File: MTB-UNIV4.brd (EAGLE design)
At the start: 100 x 80 mm, 27 parts, among them IC1 MEGA128-A, IC2 SN75176AP, IC3 NCP1117, IC4 ULN2803A, IC5 ULN2803A, X1 MKDSN1,5/4-5,08, X2 MKDSN1,5/4-5,08

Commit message: Přidány vstupní části
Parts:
- added C10, C11, C12, C13, C14, C15, C16, C17, C18, C19, C20, C21, C22, C23, C24, C9: 100nF, rcl:C1206
- added JP3, JP4: (no value), adafruit:1X08-BIG
- added R10, R11, R12, R13, R14, R15, R16, R17, R18, R3, R4, R5, R6, R7, R8, R9: 2k2, rcl:R1206
- added RN1, RN2: (no value), resistor-net:RN-9
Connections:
- new net N$21: C17.1, JP4.1, R11.2
- new net N$22: C18.1, JP4.2, R12.2
- new net N$23: C19.1, JP4.3, R13.2
- new net N$24: C20.1, JP4.4, R14.2
- new net N$25: C21.1, JP4.5, R15.2
- new net N$26: C22.1, JP4.6, R16.2
- new net N$27: C23.1, JP4.7, R17.2
- new net N$28: C24.1, JP4.8, R18.2
- new net N$29: C9.1, JP3.1, R3.2
- new net N$30: C10.1, JP3.2, R4.2
- new net N$31: C11.1, JP3.3, R5.2
- new net N$32: C12.1, JP3.4, R6.2
- new net N$33: C13.1, JP3.5, R7.2
- new net N$34: C14.1, JP3.6, R8.2
- new net N$35: C15.1, JP3.7, R9.2
- new net N$36: C16.1, JP3.8, R10.2
- net +5V: now also RN1.1, RN2.1
- net D-IN(A)1: now also R3.1, RN1.9
- net D-IN(A)2: now also R4.1, RN1.8
- net D-IN(A)3: now also R5.1, RN1.7
- net D-IN(A)4: now also R6.1, RN1.6
- net D-IN(A)5: now also R7.1, RN1.5
- net D-IN(A)6: now also R8.1, RN1.4
- net D-IN(A)7: now also R9.1, RN1.3
- net D-IN(A)8: now also R10.1, RN1.2
- net D-IN(B)1: now also R11.1, RN2.9
- net D-IN(B)2: now also R12.1, RN2.8
- net D-IN(B)3: now also R13.1, RN2.7
- net D-IN(B)4: now also R14.1, RN2.6
- net D-IN(B)5: now also R15.1, RN2.5
- net D-IN(B)6: now also R16.1, RN2.4
- net D-IN(B)7: now also R17.1, RN2.3
- net D-IN(B)8: now also R18.1, RN2.2
- net GND: now also C10.2, C11.2, C12.2, C13.2, C14.2, C15.2, C16.2, C17.2, C18.2, C19.2, C20.2, C21.2, C22.2, C23.2, C24.2, C9.2

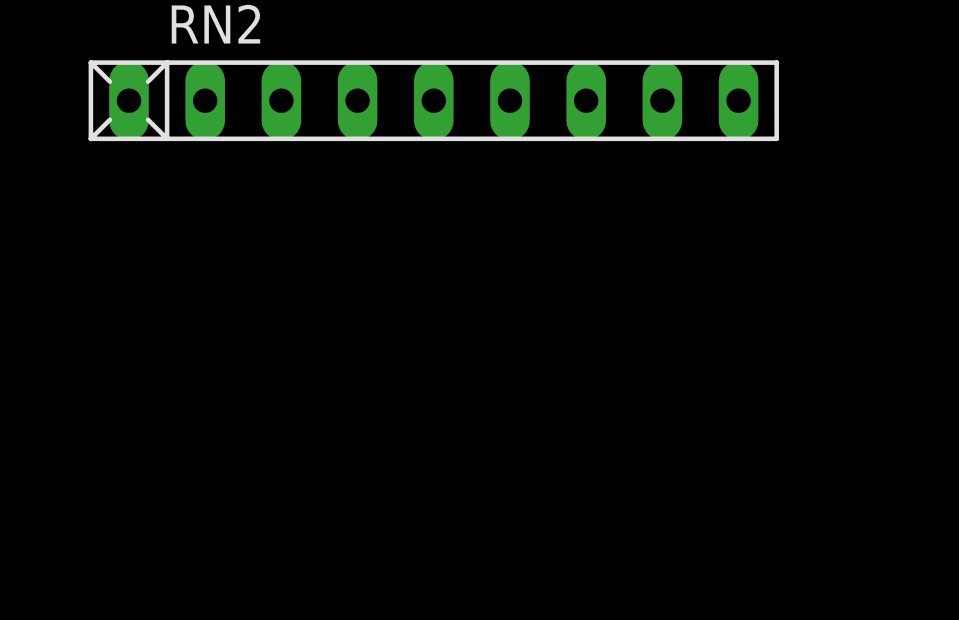
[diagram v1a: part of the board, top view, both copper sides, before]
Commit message: Přidány jumpery pro adresaci na sběrnici
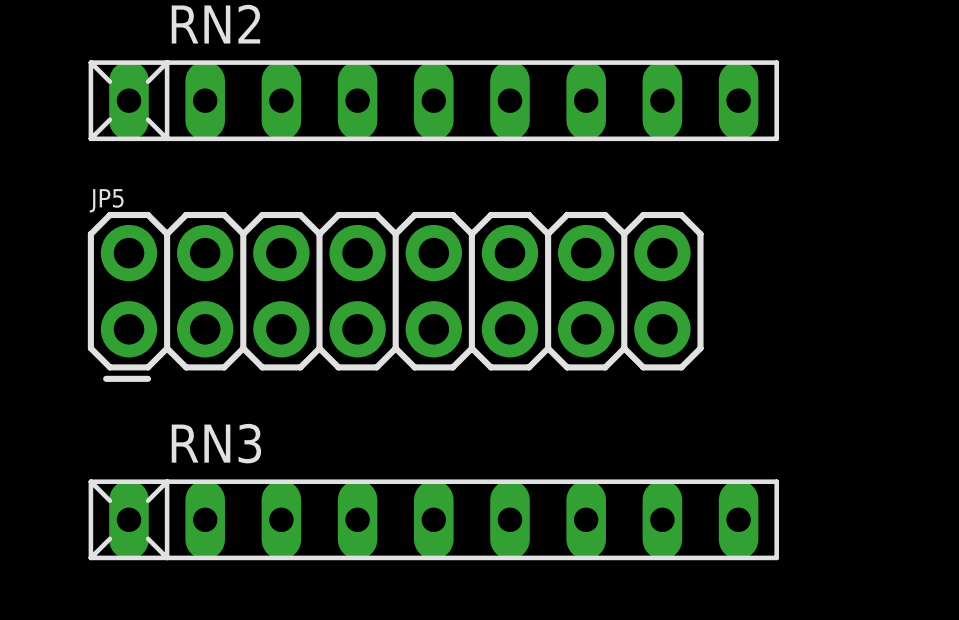
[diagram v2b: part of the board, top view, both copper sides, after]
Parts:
- added JP5: (no value), SparkFun-Connectors:2X8
- added RN3: 10k, resistor-net:RN-9
- RN1, RN2: value (none) -> 10k
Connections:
- new net ADDR-1: IC1.5, JP5.1, RN3.9
- new net ADDR-2: IC1.6, JP5.3, RN3.8
- new net ADDR-3: IC1.7, JP5.5, RN3.7
- new net ADDR-4: IC1.8, JP5.7, RN3.6
- new net ADDR-5: IC1.9, JP5.9, RN3.5
- new net ADDR-6: IC1.10, JP5.11, RN3.4
- new net ADDR-7: IC1.14, JP5.13, RN3.3
- new net ADDR-8: IC1.15, JP5.15, RN3.2
- net +5V: now also RN3.1
- net GND: now also JP5.10, JP5.12, JP5.14, JP5.16, JP5.2, JP5.4, JP5.6, JP5.8
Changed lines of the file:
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@@
 <layer number="112" name="tSilk" color="7" fill="1" visible="no" active="yes"/>
 <layer number="113" name="ReferenceLS" color="7" fill="1" visible="no" active="no"/>
+<layer number="114" name="Badge_Outline" color="7" fill="1" visible="yes" active="yes"/>
+<layer number="115" name="ReferenceISLANDS" color="7" fill="1" visible="yes" active="yes"/>
 <layer number="116" name="Patch_BOT" color="9" fill="4" visible="no" active="yes"/>
 <layer number="118" name="Rect_Pads" color="7" fill="1" visible="no" active="no"/>
@@
 <attribute name="VALUE" x="-74.93" y="-422.91" size="1.27" layer="27"/>
 </element>
-<element name="RN1" library="resistor-net" library_urn="urn:adsk.eagle:library:343" package="RN-9" package3d_urn="urn:adsk.eagle:package:24977/1" value="" x="-64.77" y="-427.99" smashed="yes">
+<element name="RN1" library="resistor-net" library_urn="urn:adsk.eagle:library:343" package="RN-9" package3d_urn="urn:adsk.eagle:package:24977/1" value="10k" x="-64.77" y="-427.99" smashed="yes">
 <attribute name="MF" value="" x="-64.77" y="-427.99" size="1.778" layer="27" display="off"/>
 <attribute name="MPN" value="" x="-64.77" y="-427.99" size="1.778" layer="27" display="off"/>
@@
 <attribute name="VALUE" x="-73.66" y="-431.165" size="1.27" layer="27" ratio="10"/>
 </element>
-<element name="RN2" library="resistor-net" library_urn="urn:adsk.eagle:library:343" package="RN-9" package3d_urn="urn:adsk.eagle:package:24977/1" value="" x="-64.77" y="-434.34" smashed="yes">
+<element name="RN2" library="resistor-net" library_urn="urn:adsk.eagle:library:343" package="RN-9" package3d_urn="urn:adsk.eagle:package:24977/1" value="10k" x="-64.77" y="-434.34" smashed="yes">
 <attribute name="MF" value="" x="-64.77" y="-434.34" size="1.778" layer="27" display="off"/>
 <attribute name="MPN" value="" x="-64.77" y="-434.34" size="1.778" layer="27" display="off"/>
@@
 <attribute name="POPULARITY" value="1" x="-64.77" y="-434.34" size="1.778" layer="27" display="off"/>
 <attribute name="VALUE" x="-73.66" y="-437.515" size="1.27" layer="27" ratio="10"/>
+</element>
+<element name="JP5" library="SparkFun-Connectors" library_urn="urn:adsk.eagle:library:513" package="2X8" package3d_urn="urn:adsk.eagle:package:38152/1" value="" x="-74.93" y="-441.96" smashed="yes">
+<attribute name="NAME" x="-76.2" y="-437.896" size="0.6096" layer="25" font="vector" ratio="20"/>
+<attribute name="VALUE" x="-76.2" y="-444.373" size="0.6096" layer="27" font="vector" ratio="20"/>
+</element>
+<element name="RN3" library="resistor-net" library_urn="urn:adsk.eagle:library:343" package="RN-9" package3d_urn="urn:adsk.eagle:package:24977/1" value="10k" x="-64.77" y="-448.31" smashed="yes">
+<attribute name="MF" value="" x="-64.77" y="-448.31" size="1.778" layer="27" display="off"/>
+<attribute name="MPN" value="" x="-64.77" y="-448.31" size="1.778" layer="27" display="off"/>
+<attribute name="NAME" x="-73.66" y="-446.405" size="1.27" layer="25" ratio="10"/>
+<attribute name="OC_FARNELL" value="unknown" x="-64.77" y="-448.31" size="1.778" layer="27" display="off"/>
+<attribute name="OC_NEWARK" value="unknown" x="-64.77" y="-448.31" size="1.778" layer="27" display="off"/>
+<attribute name="POPULARITY" value="1" x="-64.77" y="-448.31" size="1.778" layer="27" display="off"/>
+<attribute name="VALUE" x="-73.66" y="-451.485" size="1.27" layer="27" ratio="10"/>
 </element>
 </elements>
@@
 <contactref element="C23" pad="2"/>
 <contactref element="C24" pad="2"/>
+<contactref element="JP5" pad="16"/>
+<contactref element="JP5" pad="14"/>
+<contactref element="JP5" pad="12"/>
+<contactref element="JP5" pad="10"/>
+<contactref element="JP5" pad="8"/>
+<contactref element="JP5" pad="6"/>
+<contactref element="JP5" pad="4"/>
+<contactref element="JP5" pad="2"/>
+<wire x1="-64.77" y1="-439.42" x2="-67.31" y2="-439.42" width="0" layer="19" extent="1-1"/>
+<wire x1="-62.23" y1="-439.42" x2="-64.77" y2="-439.42" width="0" layer="19" extent="1-1"/>
+<wire x1="-59.69" y1="-439.42" x2="-62.23" y2="-439.42" width="0" layer="19" extent="1-1"/>
+<wire x1="-57.15" y1="-439.42" x2="-59.69" y2="-439.42" width="0" layer="19" extent="1-1"/>
+<wire x1="-69.85" y1="-439.42" x2="-67.31" y2="-439.42" width="0" layer="19" extent="1-1"/>
+<wire x1="-72.39" y1="-439.42" x2="-69.85" y2="-439.42" width="0" layer="19" extent="1-1"/>
+<wire x1="-74.93" y1="-439.42" x2="-72.39" y2="-439.42" width="0" layer="19" extent="1-1"/>
+<wire x1="-72.26" y1="-420.37" x2="-72.39" y2="-439.42" width="0" layer="19" extent="1-1"/>
 <wire x1="-72.26" y1="-414.02" x2="-72.26" y2="-420.37" width="0" layer="19" extent="1-1"/>
 <wire x1="-72.26" y1="-407.67" x2="-72.26" y2="-414.02" width="0" layer="19" extent="1-1"/>
@@
 <contactref element="RN2" pad="1"/>
 <contactref element="RN1" pad="1"/>
+<contactref element="RN3" pad="1"/>
 <wire x1="-74.93" y1="-434.34" x2="-74.93" y2="-427.99" width="0" layer="19" extent="1-1"/>
+<wire x1="-74.93" y1="-448.31" x2="-74.93" y2="-434.34" width="0" layer="19" extent="1-1"/>
 <wire x1="-75.06" y1="-199.39" x2="-74.93" y2="-427.99" width="0" layer="19" extent="1-1"/>
 <wire x1="-76.43" y1="-184.15" x2="-75.06" y2="-199.39" width="0" layer="19" extent="1-1"/>
@@
 <wire x1="-57.15" y1="-207.01" x2="-72.238" y2="-267.97" width="0" layer="19" extent="1-1"/>
 </signal>
+<signal name="ADDR-1">
+<contactref element="IC1" pad="5"/>
+<contactref element="JP5" pad="1"/>
+<contactref element="RN3" pad="9"/>
+<wire x1="-74.93" y1="-441.96" x2="-54.61" y2="-448.31" width="0" layer="19" extent="1-1"/>
+<wire x1="-26.85" y1="-18.79" x2="-74.93" y2="-441.96" width="0" layer="19" extent="1-1"/>
+</signal>
+<signal name="ADDR-2">
+<contactref element="IC1" pad="6"/>
+<contactref element="JP5" pad="3"/>
+<contactref element="RN3" pad="8"/>
+<wire x1="-72.39" y1="-441.96" x2="-57.15" y2="-448.31" width="0" layer="19" extent="1-1"/>
+<wire x1="-26.85" y1="-19.59" x2="-72.39" y2="-441.96" width="0" layer="19" extent="1-1"/>
+</signal>
+<signal name="ADDR-3">
+<contactref element="IC1" pad="7"/>
+<contactref element="JP5" pad="5"/>
+<contactref element="RN3" pad="7"/>
+<wire x1="-69.85" y1="-441.96" x2="-59.69" y2="-448.31" width="0" layer="19" extent="1-1"/>
+<wire x1="-26.85" y1="-20.39" x2="-69.85" y2="-441.96" width="0" layer="19" extent="1-1"/>
+</signal>
+<signal name="ADDR-4">
+<contactref element="IC1" pad="8"/>
+<contactref element="JP5" pad="7"/>
+<contactref element="RN3" pad="6"/>
+<wire x1="-67.31" y1="-441.96" x2="-26.85" y2="-21.19" width="0" layer="19" extent="1-1"/>
+<wire x1="-62.23" y1="-448.31" x2="-67.31" y2="-441.96" width="0" layer="19" extent="1-1"/>
+</signal>
+<signal name="ADDR-5">
+<contactref element="IC1" pad="9"/>
+<contactref element="JP5" pad="9"/>
+<contactref element="RN3" pad="5"/>
+<wire x1="-64.77" y1="-448.31" x2="-64.77" y2="-441.96" width="0" layer="19" extent="1-1"/>
+<wire x1="-26.85" y1="-21.99" x2="-64.77" y2="-441.96" width="0" layer="19" extent="1-1"/>
+</signal>
+<signal name="ADDR-6">
+<contactref element="IC1" pad="10"/>
+<contactref element="JP5" pad="11"/>
+<contactref element="RN3" pad="4"/>
+<wire x1="-67.31" y1="-448.31" x2="-62.23" y2="-441.96" width="0" layer="19" extent="1-1"/>
+<wire x1="-26.85" y1="-22.79" x2="-62.23" y2="-441.96" width="0" layer="19" extent="1-1"/>
+</signal>
+<signal name="ADDR-7">
+<contactref element="IC1" pad="14"/>
+<contactref element="JP5" pad="13"/>
+<contactref element="RN3" pad="3"/>
+<wire x1="-69.85" y1="-448.31" x2="-59.69" y2="-441.96" width="0" layer="19" extent="1-1"/>
+<wire x1="-26.85" y1="-25.99" x2="-59.69" y2="-441.96" width="0" layer="19" extent="1-1"/>
+</signal>
+<signal name="ADDR-8">
+<contactref element="IC1" pad="15"/>
+<contactref element="JP5" pad="15"/>
+<contactref element="RN3" pad="2"/>
+<wire x1="-72.39" y1="-448.31" x2="-57.15" y2="-441.96" width="0" layer="19" extent="1-1"/>
+<wire x1="-26.85" y1="-26.79" x2="-57.15" y2="-441.96" width="0" layer="19" extent="1-1"/>
+</signal>
 </signals>

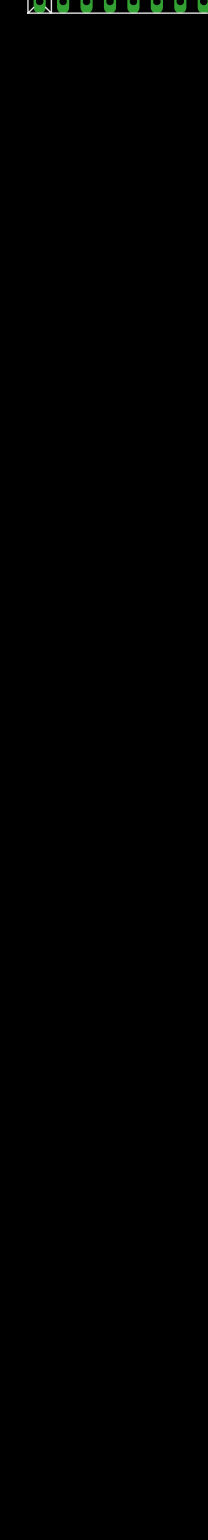
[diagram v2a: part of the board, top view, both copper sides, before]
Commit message: Nahradil jsem spojení COM na ULN Crowbar přepěťovou ochranou. Je to trochu více součástek, ale rozhodně to bude fungovat.
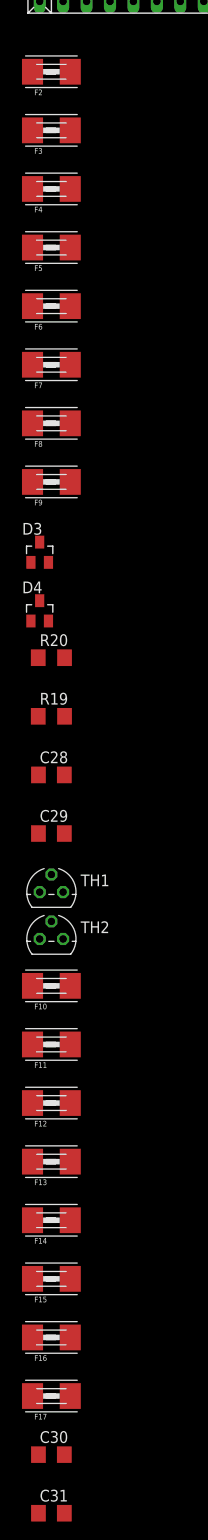
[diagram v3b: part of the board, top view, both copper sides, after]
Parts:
- added C28, C29, C30, C31: 100nF, rcl:C1206
- added D3, D4: (no value), diode:SOT23
- added F10, F11, F12, F13, F14, F15, F16, F17, F2, F3, F4, F5, F6, F7, F8, F9: (no value), adafruit:1812
- added R19, R20: 2k2, rcl:R1206
- added TH1, TH2: MCR100, ElectroKrt:TO92
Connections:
- new net N$37: C28.1, D3.3, IC4.10, TH1.3
- new net N$38: F9.1, IC4.11
- new net N$39: F8.1, IC4.12
- new net N$40: F7.1, IC4.13
- new net N$41: F6.1, IC4.14
- new net N$42: F5.1, IC4.15
- new net N$43: F4.1, IC4.16
- new net N$44: F3.1, IC4.17
- new net N$45: F2.1, IC4.18
- new net N$46: C29.1, D3.1, R19.2, TH1.2
- new net N$47: F17.2, JP2.8
- new net N$48: F17.1, IC5.11
- new net N$49: F16.1, IC5.12
- new net N$50: F15.1, IC5.13
- new net N$51: F14.1, IC5.14
- new net N$52: F13.1, IC5.15
- new net N$53: F12.1, IC5.16
- new net N$54: F11.1, IC5.17
- new net N$55: F10.1, IC5.18
- new net N$56: C31.1, D4.1, R20.2, TH2.2
- net GND: now also C28.2, C29.2, C30.2, C31.2, R19.1, R20.1, TH1.1, TH2.1; no longer IC4.10, IC5.10
- net N$10: now also F9.2, JP1.8; no longer IC4.18, JP1.1
- net N$11: now also C30.1, D4.3, IC5.10, TH2.3; no longer IC5.11, JP2.8
- net N$12: now also F10.2, JP2.1; no longer IC5.12, JP2.7
- net N$15: now also F11.2, JP2.2; no longer IC5.13, JP2.6
- net N$16: now also F12.2, JP2.3; no longer IC5.14, JP2.5
- net N$17: now also F13.2; no longer IC5.15
- net N$18: now also F14.2, JP2.5; no longer IC5.16, JP2.3
- net N$19: now also F15.2, JP2.6; no longer IC5.17, JP2.2
- net N$2: now also F2.2, JP1.1; no longer IC4.11, JP1.8
- net N$20: now also F16.2, JP2.7; no longer IC5.18, JP2.1
- net N$4: now also F3.2, JP1.2; no longer IC4.12, JP1.7
- net N$5: now also F4.2, JP1.3; no longer IC4.13, JP1.6
- net N$6: now also F5.2, JP1.4; no longer IC4.14, JP1.5
- net N$7: now also F6.2, JP1.5; no longer IC4.15, JP1.4
- net N$8: now also F7.2, JP1.6; no longer IC4.16, JP1.3
- net N$9: now also F8.2, JP1.7; no longer IC4.17, JP1.2
